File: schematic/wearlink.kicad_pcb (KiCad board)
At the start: 2 copper layers, 8 parts, among them J1 JTAG, Q1 MMBT3904, U1 WT51822-0S4AT

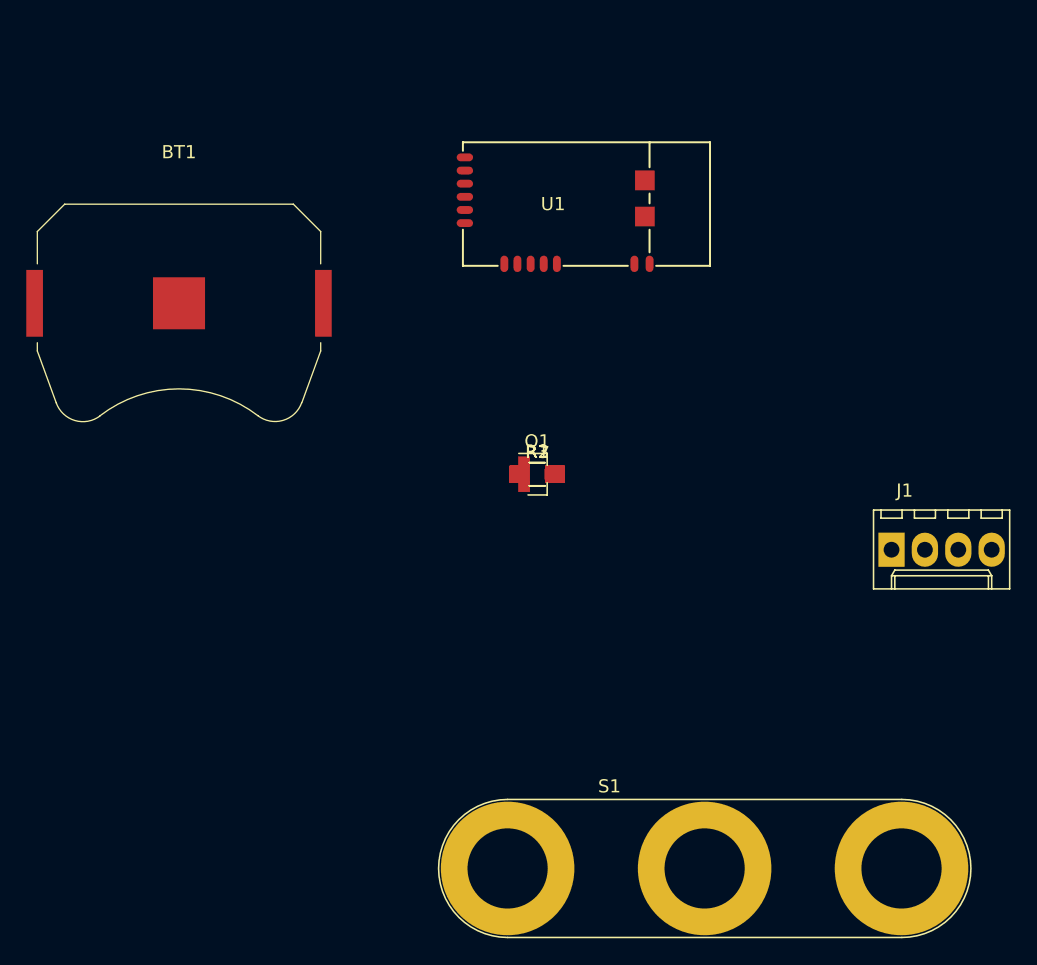
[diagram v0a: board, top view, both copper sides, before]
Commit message: Added footprints, first route
Seems a little to spacious..
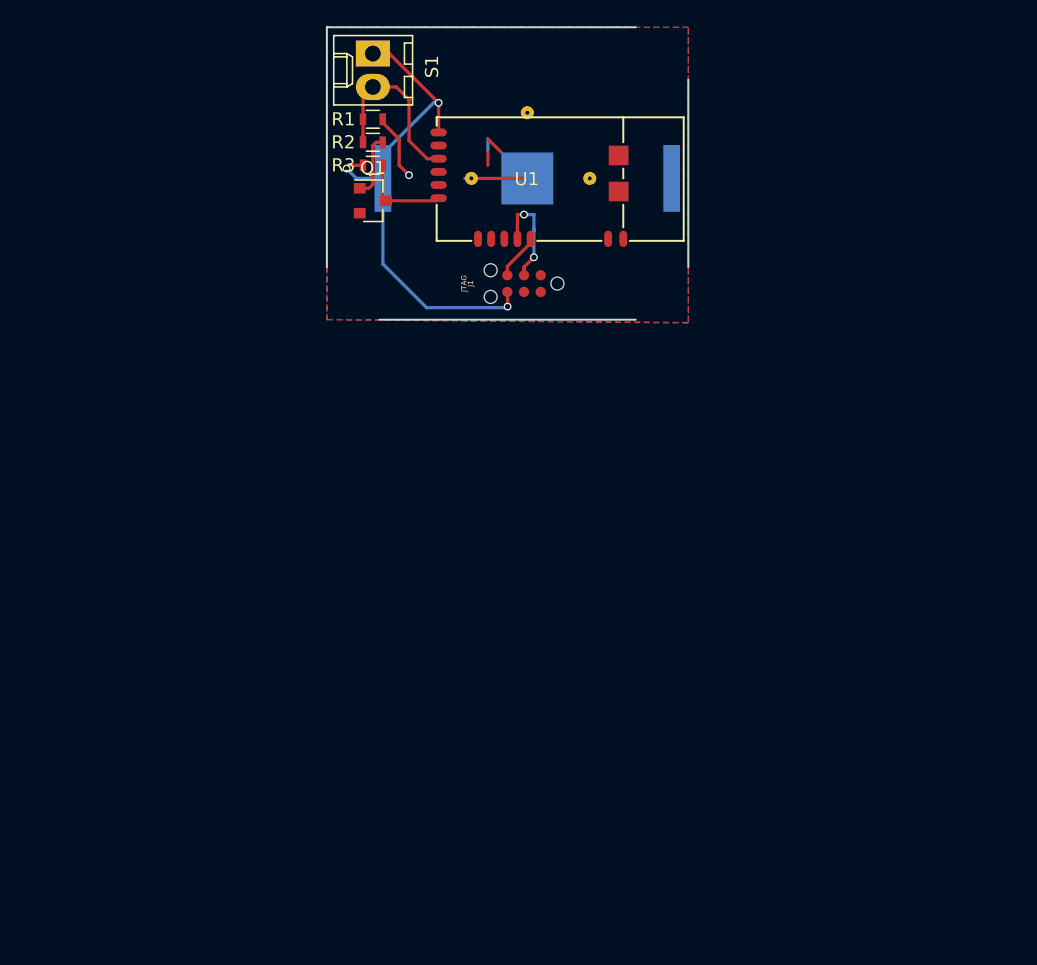
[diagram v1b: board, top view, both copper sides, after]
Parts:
- added ?: , wearlink:PVIA, F.Cu at (152.5, 82.5)
- added ?: , wearlink:PVIA, F.Cu at (147.8, 77.5)
- added ?: , wearlink:PVIA, F.Cu at (143.5, 82.5)
- BT1: value Battery_Cell -> Battery 2032; moved to B.Cu
- J1: footprint Connectors_Molex:Molex_KK-6410-04_04x2.54mm_Straight -> wearlink:TC2030-IDC-NL
- R1, R2, R3: footprint Resistors_SMD:R_0805_HandSoldering -> Resistors_SMD:R_0603
- S1: footprint Connectors:Banana_Jack_3Pin -> Connectors_Molex:Molex_KK-6410-02_02x2.54mm_Straight
- moved S1 62.8 mm to (136.0, 73.0), turned to 270 degrees
- moved J1 34.5 mm to (147.5, 90.5), turned to 270 degrees
- moved R1 29.8 mm to (136.0, 78.0)
- moved R2 28.2 mm to (136.0, 79.8), turned to 180 degrees
- moved BT1 28.2 mm to (147.8, 82.5), turned to 180 degrees
- moved R3 26.6 mm to (136.0, 81.5)
- moved Q1 24.3 mm to (136.0, 84.2)
- moved U1 2.76 mm to (150.2, 82.5)
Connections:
- BT1 pad 2: Net-(BT1-Pad2) -> GND
- J1 pad 1: Net-(BT1-Pad2) -> (no net)
- J1 pad 2: Net-(J1-Pad2) -> GND
- J1 pad 4: POWER -> GND
- Q1 pad 2: Net-(BT1-Pad2) -> GND
- R1 pad 2: Net-(BT1-Pad2) -> GND
- U1 pad 11: Net-(J1-Pad2) -> Net-(J1-Pad5)
- U1 pad 12: Net-(BT1-Pad2) -> GND
- U1 pad 13: Net-(BT1-Pad2) -> GND
- U1 pad 14: Net-(BT1-Pad2) -> GND
- U1 pad 15: Net-(BT1-Pad2) -> GND
- U1 pad 2: Net-(BT1-Pad2) -> GND
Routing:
- net POWER: track 0.00 -> 39.5 mm, vias 0 -> 3
- net ADC: track 0.00 -> 14.3 mm
- net Net-(J1-Pad3): track 0.00 -> 8.47 mm, vias 0 -> 2
- net (no net): track 0.00 -> 7.91 mm
- net SENSE: track 0.00 -> 6.89 mm
- net GND: track 0.00 -> 5.08 mm, vias 0 -> 1
- net Net-(Q1-Pad1): track 0.00 -> 4.93 mm
- net Net-(J1-Pad5): track 0.00 -> 3.50 mm
- added copper zone on B.Cu, net GND
- added copper zone on F.Cu, net GND
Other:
- board outline added: 27.5 x 22.2 mm

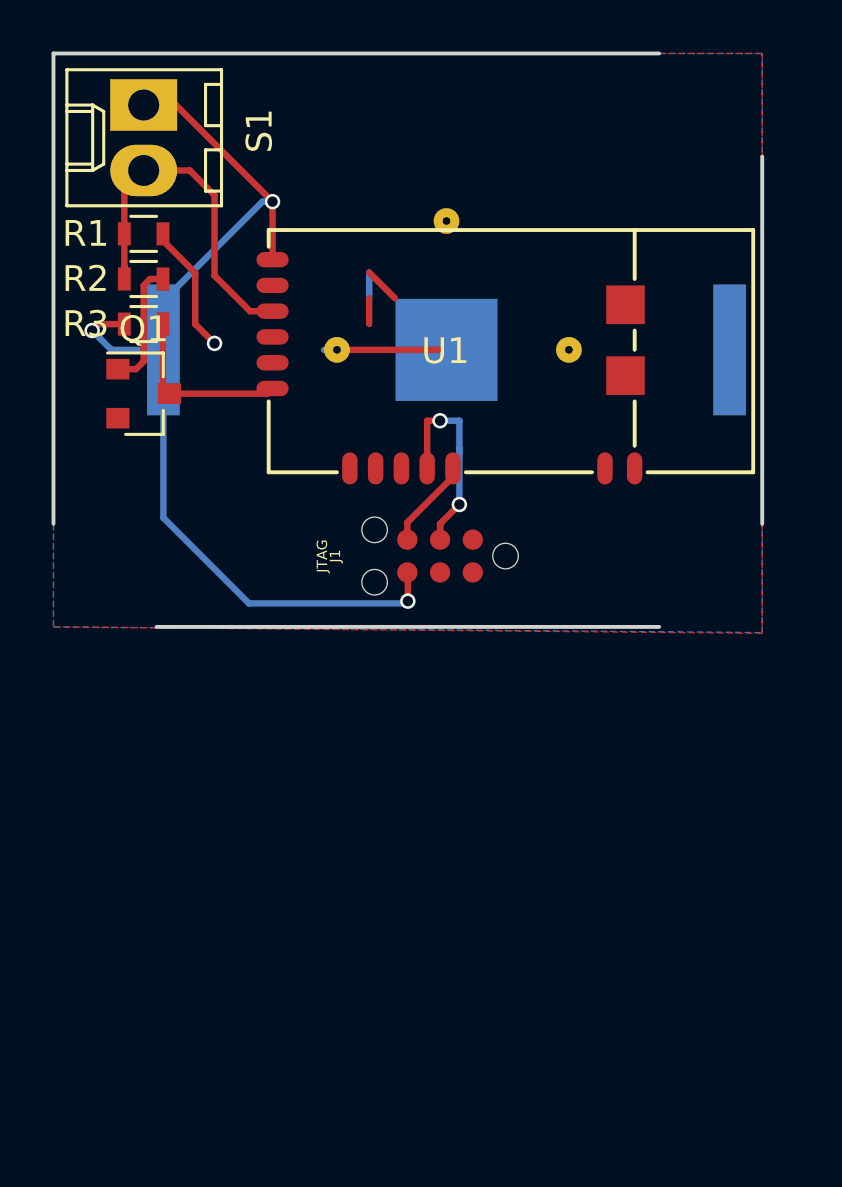
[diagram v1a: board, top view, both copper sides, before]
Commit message: Cleaned up schematic
Added holes for module
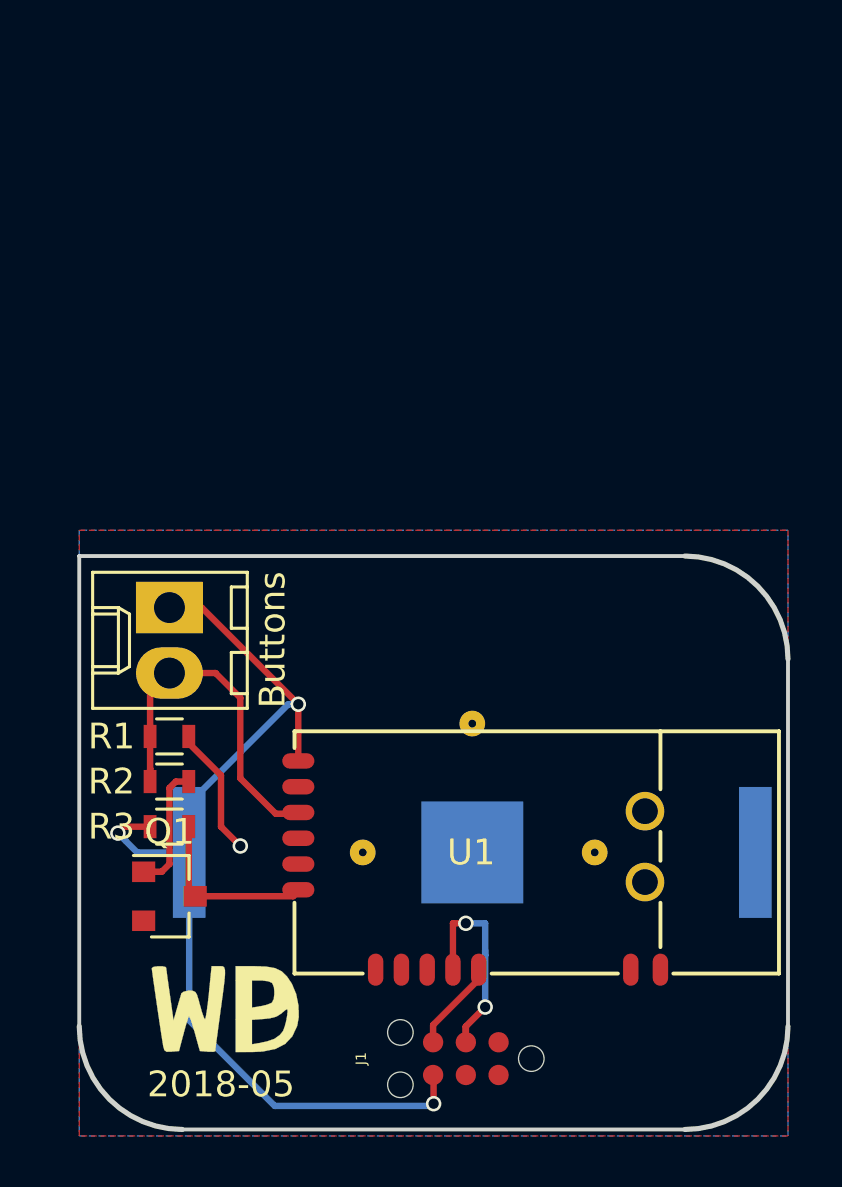
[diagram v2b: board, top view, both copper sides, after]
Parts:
- removed the ? at (147.8, 77.5)
- removed the ? at (143.5, 82.5)
- added ?: , wearlink:PVIA, F.Cu at (144.5, 102.0)
- added ?: , wearlink:PVIA, F.Cu at (148.8, 97.0)
- added G***: LOGO, wearlink:wpd, F.Cu at (139.2, 108.0)
- moved ? 19.5 mm to (153.5, 102.0)
- moved BT1 19.5 mm to (148.8, 102.0)
- moved Buttons 19.5 mm to (137.0, 92.5)
- moved J1 19.5 mm to (148.5, 110.0)
- moved Q1 19.5 mm to (137.0, 103.7)
- moved R1 19.5 mm to (137.0, 97.5)
- moved R2 19.5 mm to (137.0, 99.2)
- moved R3 19.5 mm to (137.0, 101.0)
- moved U1 19.5 mm to (151.2, 102.0)
- renumbered S1 to Buttons
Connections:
- ? pad : (no net) -> GND
- U1 pad 1: POWER -> (no net)
- U1 pad 10: Net-(J1-Pad3) -> (no net)
- U1 pad 11: Net-(J1-Pad5) -> (no net)
- U1 pad 12: GND -> (no net)
- U1 pad 13: GND -> (no net)
- U1 pad 14: GND -> (no net)
- U1 pad 15: GND -> (no net)
- U1 pad 2: GND -> (no net)
- U1 pad 3: ADC -> (no net)
- U1 pad 6: SENSE -> (no net)
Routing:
- net (no net): track 7.91 -> 0.00 mm
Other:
- board text added: "2018-05"

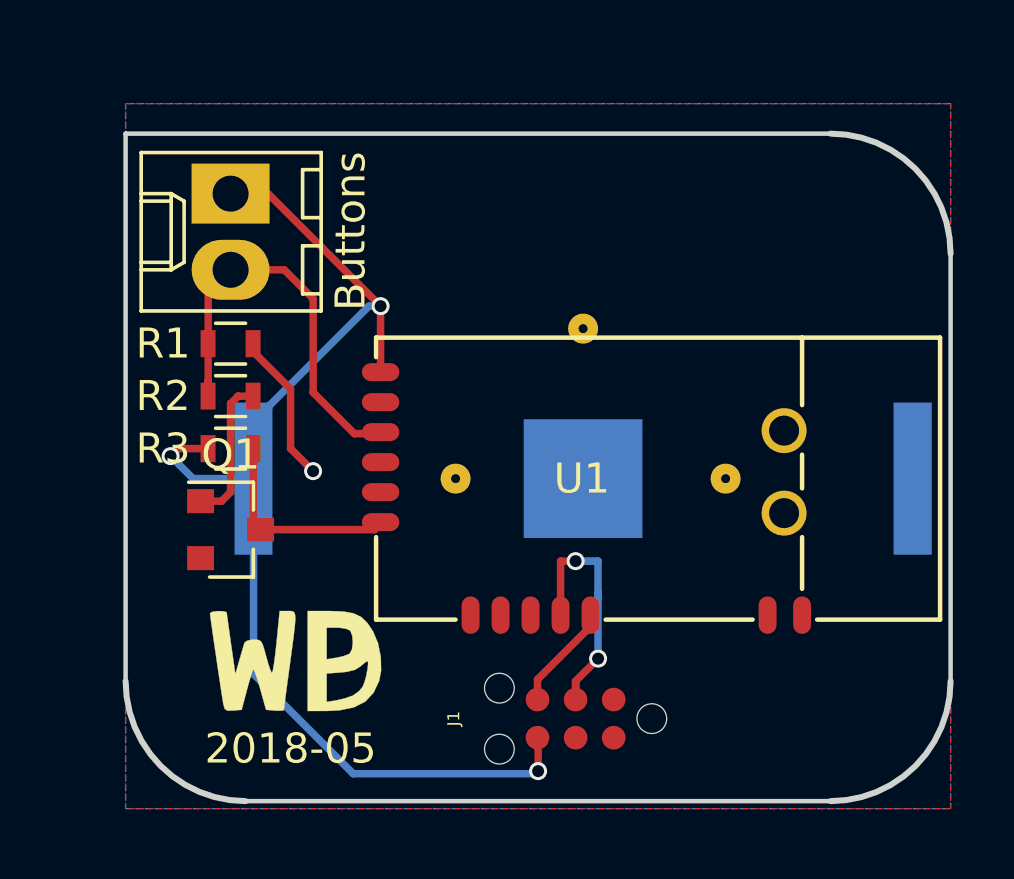
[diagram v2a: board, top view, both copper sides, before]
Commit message: Made pcb smaller
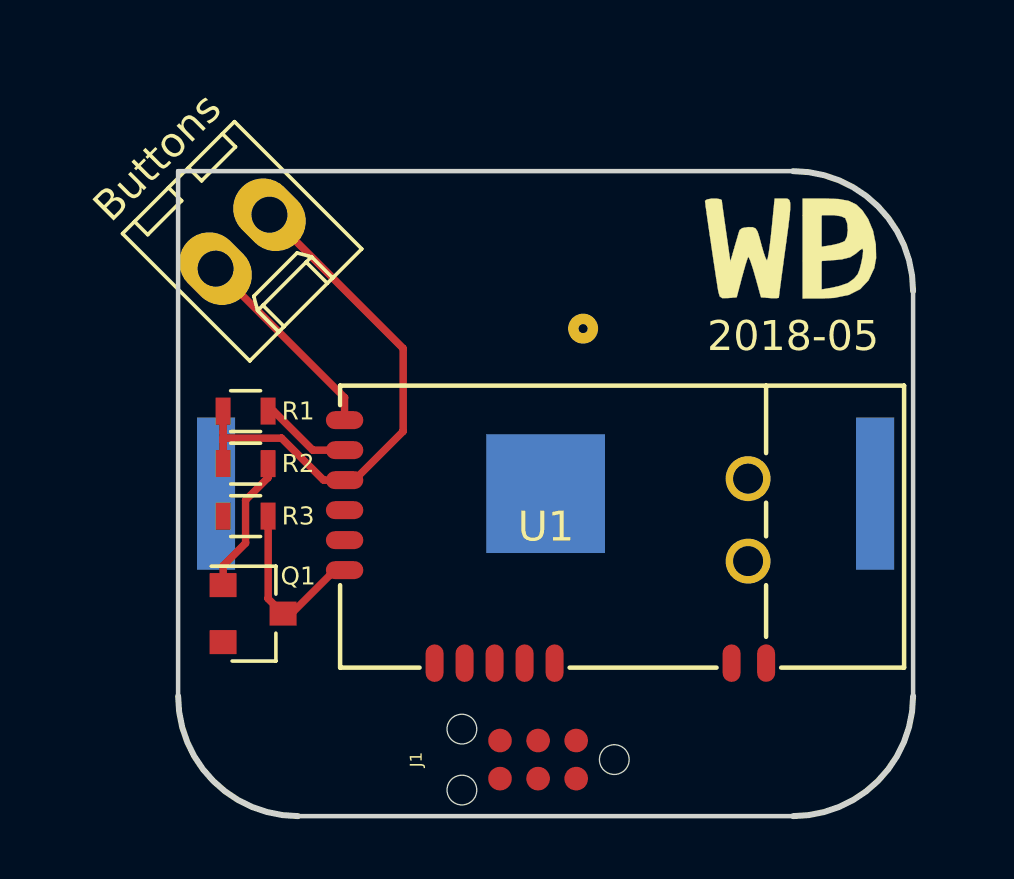
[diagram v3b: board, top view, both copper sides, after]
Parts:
- removed the ? at (144.5, 102.0)
- removed the ? at (153.5, 102.0)
- moved G*** 21.5 mm to (155.8, 94.2)
- moved Q1 2.90 mm to (137.8, 106.5)
- moved Buttons 2.55 mm to (136.5, 95.0), turned to 45 degrees
- moved R1 2.30 mm to (137.5, 99.8)
- moved R2 2.30 mm to (137.5, 101.5)
- moved R3 2.30 mm to (137.5, 103.2)
- moved U1 2.00 mm to (150.1, 103.6)
- moved J1 1.85 mm to (147.2, 111.4)
- moved BT1 1.35 mm to (147.5, 102.5)
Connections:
- U1 pad 1: (no net) -> POWER
- U1 pad 10: (no net) -> Net-(J1-Pad3)
- U1 pad 11: (no net) -> Net-(J1-Pad5)
- U1 pad 12: (no net) -> GND
- U1 pad 13: (no net) -> GND
- U1 pad 14: (no net) -> GND
- U1 pad 15: (no net) -> GND
- U1 pad 2: (no net) -> GND
- U1 pad 3: (no net) -> ADC
- U1 pad 6: (no net) -> SENSE
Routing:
- net POWER: track 39.5 -> 6.83 mm, vias 3 -> 0
- net Net-(J1-Pad3): track 8.47 -> 0.00 mm, vias 2 -> 0
- net ADC: track 14.3 -> 18.3 mm
- net Net-(J1-Pad5): track 3.50 -> 0.00 mm
- net GND: track 5.08 -> 3.09 mm, vias 1 -> 0
- net SENSE: track 6.89 -> 6.11 mm
- removed copper zone on B.Cu, net GND
- removed copper zone on F.Cu, net GND
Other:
- board size 27.5 x 22.2 mm -> 24.5 x 21.5 mm

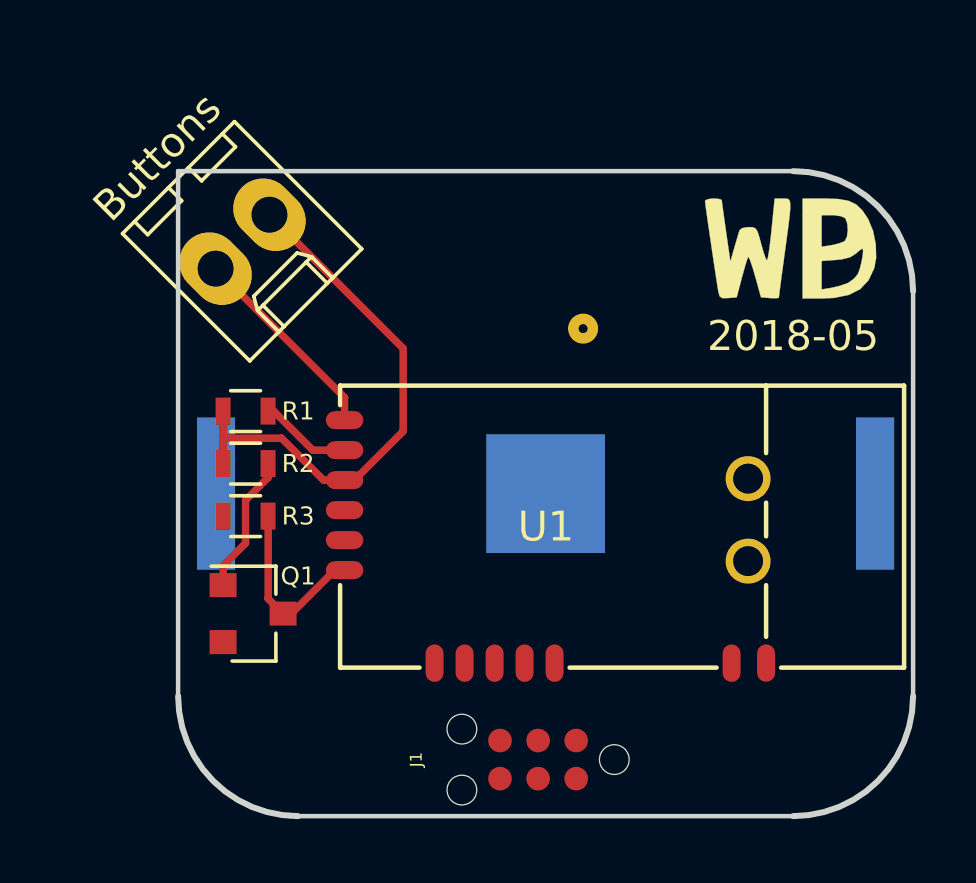
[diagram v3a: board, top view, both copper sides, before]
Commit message: Verified hole sizes WT51822, more pcb cleanup
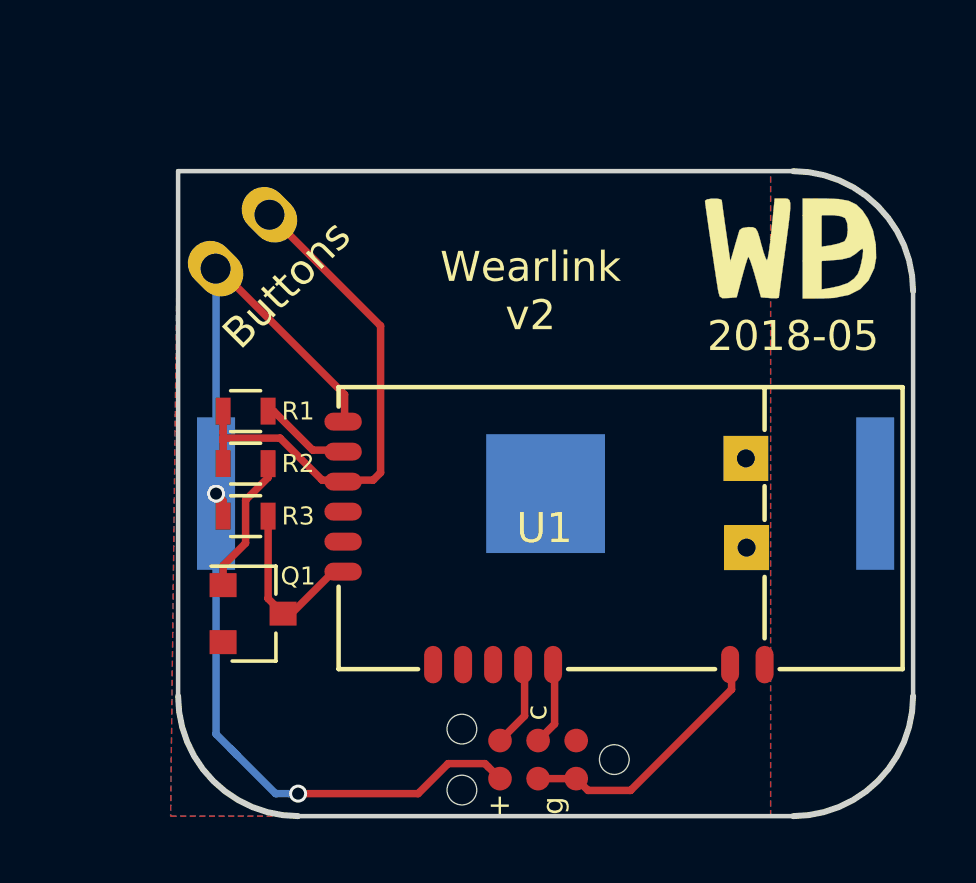
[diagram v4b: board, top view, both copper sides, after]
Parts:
- removed ?: , wearlink:PVIA
- Buttons: footprint Connectors_Molex:Molex_KK-6410-02_02x2.54mm_Straight -> wearlink:FibretronicKeypad
- moved U1 0.07 mm to (150.0, 103.7)
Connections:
- U1 pad 10: Net-(J1-Pad3) -> Net-(J1-Pad5)
- U1 pad 11: Net-(J1-Pad5) -> Net-(J1-Pad3)
- U1 pad 14: GND -> (no net)
- U1 pad 15: GND -> (no net)
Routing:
- net POWER: track 6.83 -> 34.4 mm, vias 0 -> 2
- net GND: track 3.09 -> 12.0 mm
- net Net-(J1-Pad5): track 0.00 -> 2.92 mm
- net Net-(J1-Pad3): track 0.00 -> 2.81 mm
- added copper zone on B.Cu, net GND
- added copper zone on F.Cu, net GND
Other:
- board text added: "+"
- board text added: "Wearlink v2"
- board text added: "c"
- board text added: "g"
